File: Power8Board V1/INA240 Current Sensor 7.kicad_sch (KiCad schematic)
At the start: 3 parts, among them U10 INA240A2PWR

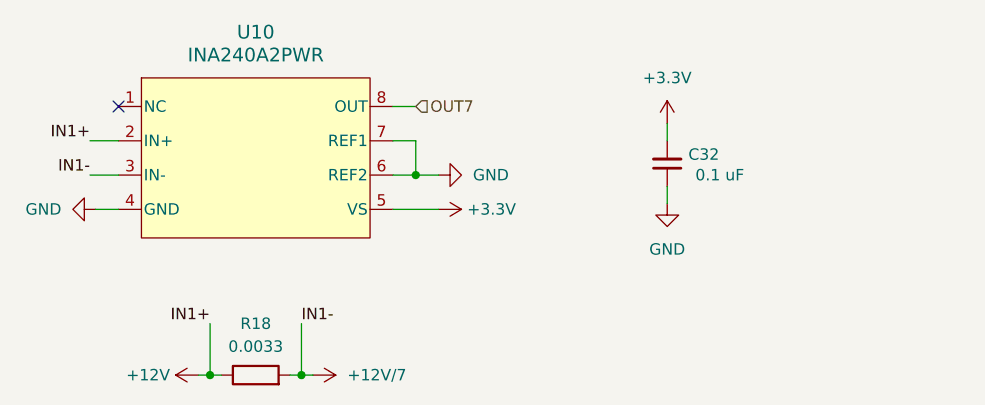
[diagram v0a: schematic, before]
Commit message: Laid out components
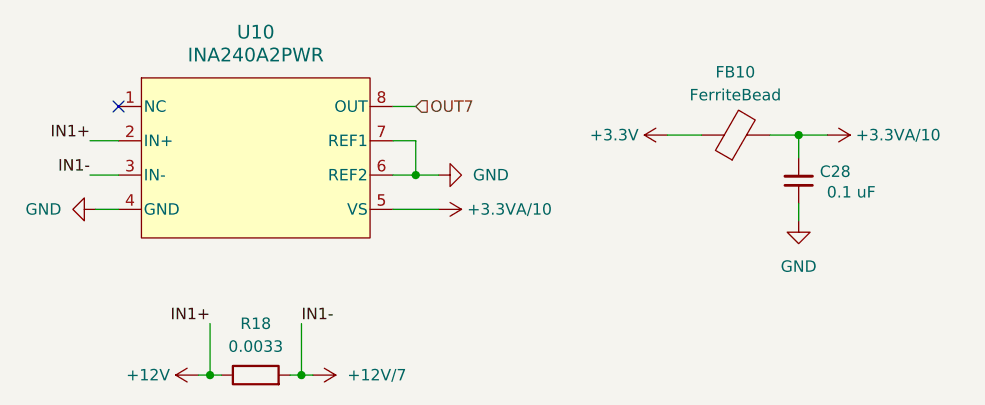
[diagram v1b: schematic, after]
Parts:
- removed C32: 0.1 uF, 0805 Ceramic Capacitor:CAPC2012X140N, symbol Device:C_Small
- added C28: 0.1 uF, 0805 Ceramic Capacitor:CAPC2012X140N, symbol Device:C_Small
- added FB10: FerriteBead, MPZ2012S102ATD25:BEADC2012X105N, symbol Device:FerriteBead
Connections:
- net +3.3V: now also FB10.1; no longer U10.5 (VS)
- net GND: now also C28.1
- new net +3.3VA/10: C28.2, FB10.2, U10.5 (VS)
